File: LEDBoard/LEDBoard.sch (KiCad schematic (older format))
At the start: 0 parts

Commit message: added the LED board
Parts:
- added D?: LED-Green, symbol LED
- added R?: R, symbol R
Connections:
- new net: D?.2 (A), R?.2
- new net SOT2/Vout: D?.1 (K)
- new net VCC: R?.1
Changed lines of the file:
@@
 $Descr A4 11693 8268
 encoding utf-8
-Sheet 1 1
+Sheet 1 2
 Title "LED Board"
 Date "11-26-16"
@@
 Comment4 ""
 $EndDescr
+$Sheet
+S 2900 1800 700  500
+U 583A699B
+F0 "SOT2" 60
+F1 "SOT2.sch" 60
+F2 "Vin +" I L 2900 1900 60
+F3 "GND" I L 2900 2050 60
+F4 "Vin -" I L 2900 2200 60
+F5 "Vcc" I R 3600 1900 60
+F6 "Vout" O R 3600 2150 60
+$EndSheet
+$Comp
+L LED D?
+U 1 1 583A7260
+P 4250 2150
+F 0 "D?" H 4250 2250 50  0000 C CNN
+F 1 "LED-Green" H 4250 2050 50  0000 C CNN
+F 2 "" H 4250 2150 50  0000 C CNN
+F 3 "" H 4250 2150 50  0000 C CNN
+	1    4250 2150
+	1    0    0    -1
+$EndComp
+$Comp
+L R R?
+U 1 1 583A72AB
+P 5000 2150
+F 0 "R?" V 5080 2150 50  0000 C CNN
+F 1 "R" V 5000 2150 50  0000 C CNN
+F 2 "" V 4930 2150 50  0000 C CNN
+F 3 "" H 5000 2150 50  0000 C CNN
+	1    5000 2150
+	0    1    1    0
+$EndComp
+Wire Wire Line
+	4050 2150 3600 2150
+Wire Wire Line
+	4850 2150 4450 2150
+Wire Wire Line
+	5150 2150 5550 2150
+$Comp
+L VCC #PWR?
+U 1 1 583A734F
+P 5550 2150
+F 0 "#PWR?" H 5550 2000 50  0001 C CNN
+F 1 "VCC" H 5550 2300 50  0000 C CNN
+F 2 "" H 5550 2150 50  0000 C CNN
+F 3 "" H 5550 2150 50  0000 C CNN
+	1    5550 2150
+	0    1    1    0
+$EndComp
 $EndSCHEMATC

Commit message: just some updates to the LED Board
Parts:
- added BT-9V: Battery, symbol Battery
- added D?: LED-Green, symbol LED
- added R?: R, symbol R
- added U?: LM193, symbol LM193
- D?: value LED-Green -> LED-Red
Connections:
- net labels added: GND
- wire segments 3 -> 8
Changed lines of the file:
@@
 P 4250 2150
 F 0 "D?" H 4250 2250 50  0000 C CNN
-F 1 "LED-Green" H 4250 2050 50  0000 C CNN
+F 1 "LED-Red" H 4250 2050 50  0000 C CNN
 F 2 "" H 4250 2150 50  0000 C CNN
 F 3 "" H 4250 2150 50  0000 C CNN
@@
 	0    1    1    0
 $EndComp
+$Comp
+L Battery BT-9V
+U 1 1 583A7522
+P 7750 1200
+F 0 "BT-9V" H 7850 1250 50  0000 L CNN
+F 1 "Battery" H 7850 1150 50  0000 L CNN
+F 2 "" V 7750 1240 50  0000 C CNN
+F 3 "" V 7750 1240 50  0000 C CNN
+	1    7750 1200
+	0    1    1    0
+$EndComp
+$Comp
+L GND #PWR?
+U 1 1 583A756B
+P 7450 1200
+F 0 "#PWR?" H 7450 950 50  0001 C CNN
+F 1 "GND" H 7450 1050 50  0000 C CNN
+F 2 "" H 7450 1200 50  0000 C CNN
+F 3 "" H 7450 1200 50  0000 C CNN
+	1    7450 1200
+	0    1    1    0
+$EndComp
+Wire Wire Line
+	7600 1200 7450 1200
+$Comp
+L R R?
+U 1 1 583A7609
+P 5000 1850
+F 0 "R?" V 5080 1850 50  0000 C CNN
+F 1 "R" V 5000 1850 50  0000 C CNN
+F 2 "" V 4930 1850 50  0000 C CNN
+F 3 "" H 5000 1850 50  0000 C CNN
+	1    5000 1850
+	0    1    1    0
+$EndComp
+$Comp
+L LED D?
+U 1 1 583A765A
+P 4500 1850
+F 0 "D?" H 4500 1950 50  0000 C CNN
+F 1 "LED-Green" H 4500 1750 50  0000 C CNN
+F 2 "" H 4500 1850 50  0000 C CNN
+F 3 "" H 4500 1850 50  0000 C CNN
+	1    4500 1850
+	1    0    0    -1
+$EndComp
+$Comp
+L GND #PWR?
+U 1 1 583A769A
+P 4200 1850
+F 0 "#PWR?" H 4200 1600 50  0001 C CNN
+F 1 "GND" H 4200 1700 50  0000 C CNN
+F 2 "" H 4200 1850 50  0000 C CNN
+F 3 "" H 4200 1850 50  0000 C CNN
+	1    4200 1850
+	0    1    1    0
+$EndComp
+Wire Wire Line
+	5350 2150 5350 1850
+Wire Wire Line
+	5350 1850 5150 1850
+Connection ~ 5350 2150
+Wire Wire Line
+	4850 1850 4700 1850
+Wire Wire Line
+	4300 1850 4200 1850
+$Comp
+L LM193 U?
+U 1 1 583A7B90
+P 10000 1250
+F 0 "U?" H 10150 1400 50  0000 C CNN
+F 1 "LM193" H 10250 1100 50  0000 C CNN
+F 2 "" H 10000 1250 50  0000 C CNN
+F 3 "" H 10000 1250 50  0000 C CNN
+	1    10000 1250
+	1    0    0    -1
+$EndComp
 $EndSCHEMATC

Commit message: more work on the LED board
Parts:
- removed BT-9V: Battery, symbol Battery
- removed D?: LED-Red, symbol LED
- removed D?: LED-Green, symbol LED
- removed R? (x2): R, symbol R
- removed U?: LM193, symbol LM193
- added P?: connector to 9V battery, symbol CONN_01X02
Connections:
- net labels removed: GND, VCC
- wire segments 8 -> 0

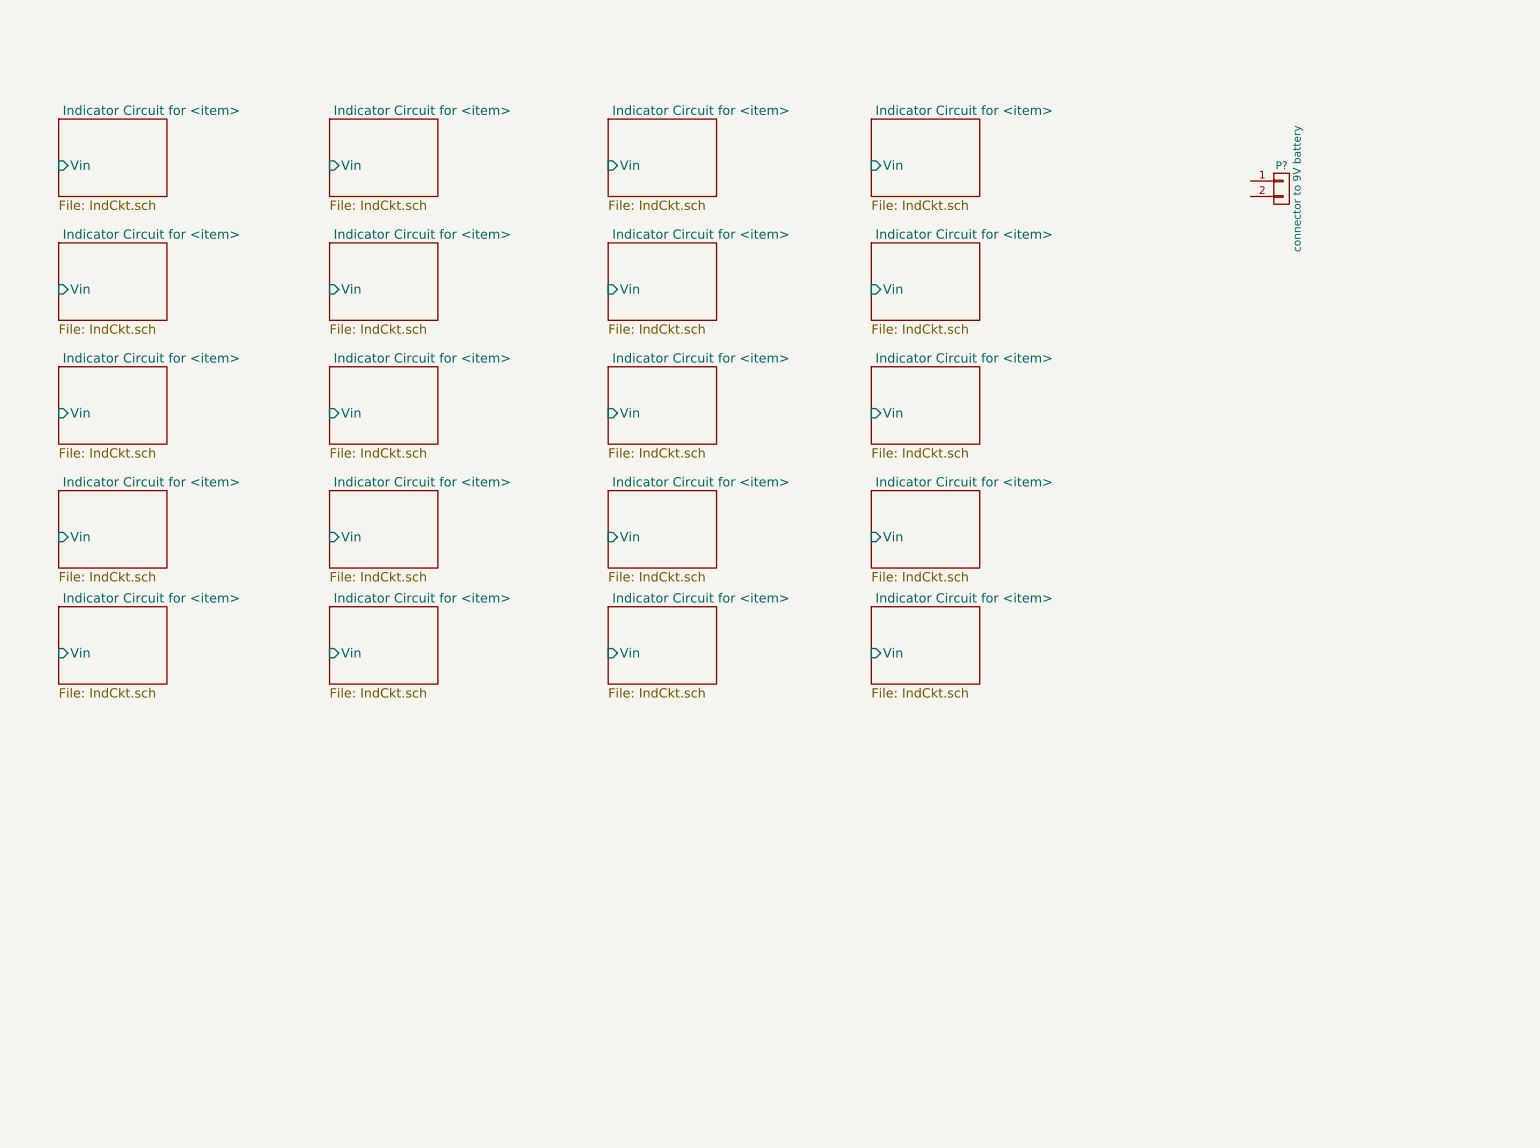
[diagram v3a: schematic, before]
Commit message: Added the power switching device and wiring between the pod batteries and backup batteries
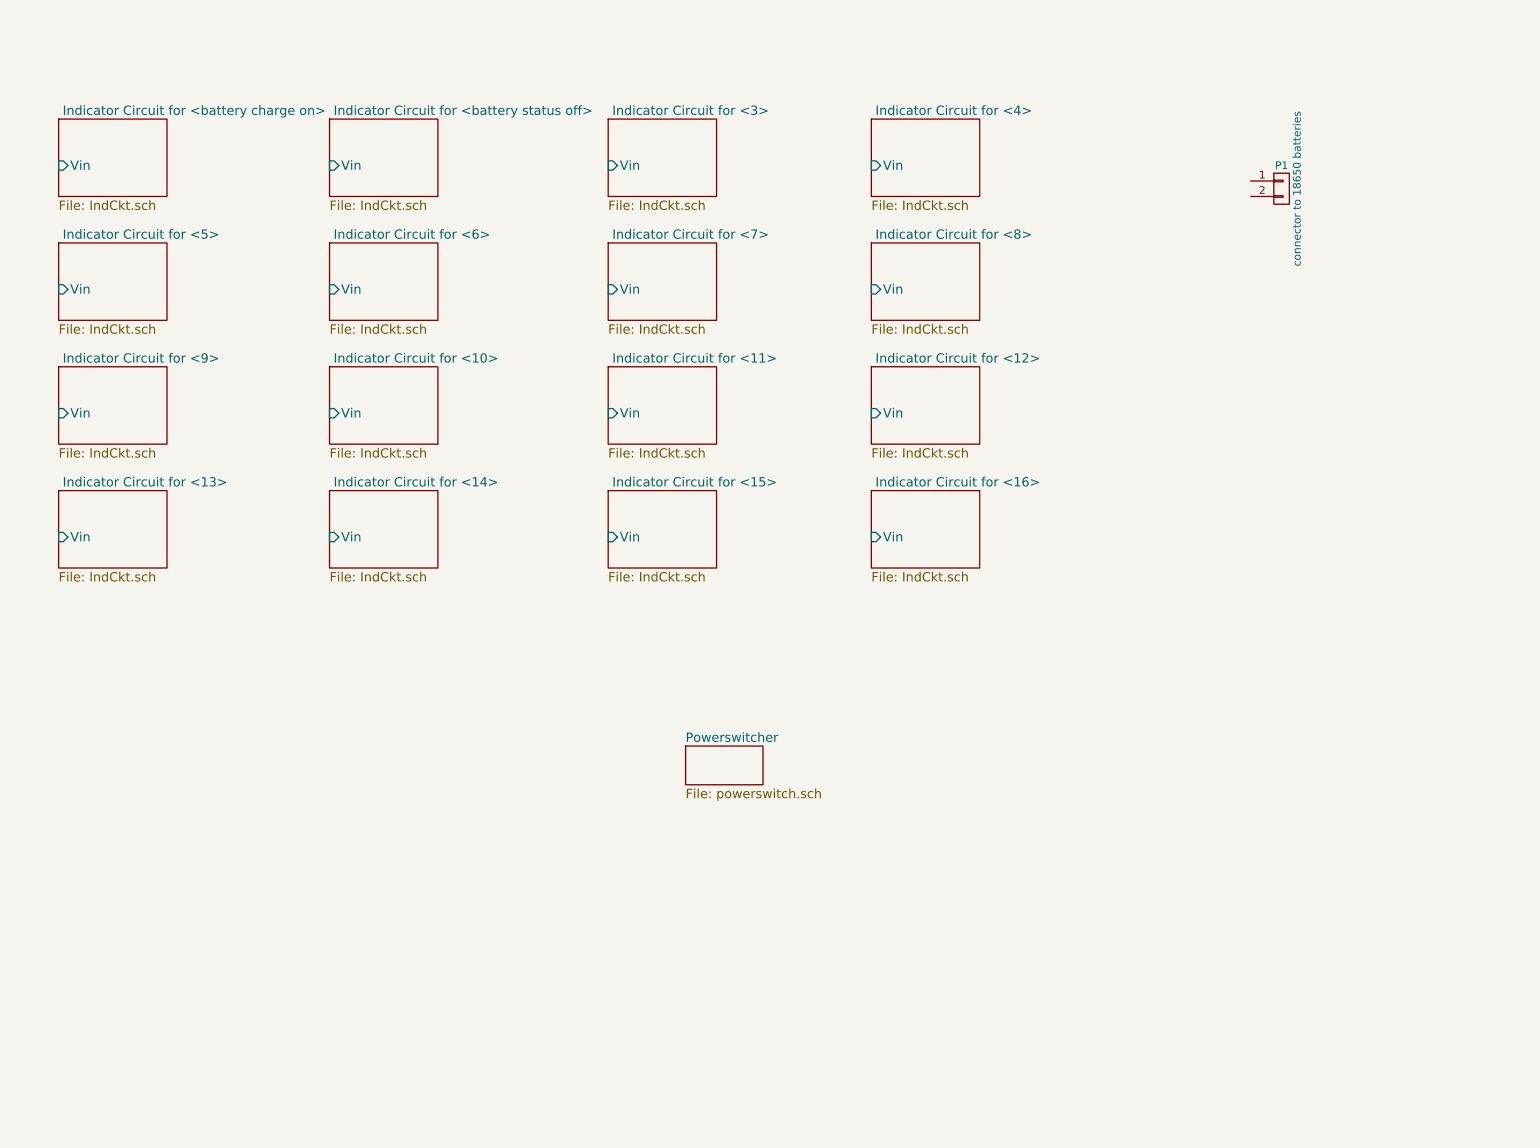
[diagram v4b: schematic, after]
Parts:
- P1: renamed from P?; value connector to 9V battery -> connector to 18650 batteries
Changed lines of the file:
@@
 LIBS:contrib
 LIBS:valves
+LIBS:SOT2-cache
 LIBS:LEDBoard-cache
 EELAYER 25 0
@@
 $Descr A4 11693 8268
 encoding utf-8
-Sheet 1 21
+Sheet 1 18
 Title "LED Board"
 Date "11-26-16"
@@
 S 1100 1300 700  500
 U 583A699B
-F0 " Indicator Circuit for <item>" 60
+F0 " Indicator Circuit for <battery charge on>" 60
 F1 "IndCkt.sch" 60
 F2 "Vin" I L 1100 1600 60
@@
 S 1100 2100 700  500
 U 583ACA1C
-F0 " Indicator Circuit for <item>" 60
+F0 " Indicator Circuit for <5>" 60
 F1 "IndCkt.sch" 60
 F2 "Vin" I L 1100 2400 60
@@
 S 1100 2900 700  500
 U 583ACAFB
-F0 " Indicator Circuit for <item>" 60
+F0 " Indicator Circuit for <9>" 60
 F1 "IndCkt.sch" 60
 F2 "Vin" I L 1100 3200 60
@@
 S 1100 3700 700  500
 U 583ACAFE
-F0 " Indicator Circuit for <item>" 60
+F0 " Indicator Circuit for <13>" 60
 F1 "IndCkt.sch" 60
 F2 "Vin" I L 1100 4000 60
 $EndSheet
 $Sheet
-S 1100 4450 700  500
-U 583ACB74
-F0 " Indicator Circuit for <item>" 60
-F1 "IndCkt.sch" 60
-F2 "Vin" I L 1100 4750 60
-$EndSheet
-$Sheet
 S 2850 1300 700  500
 U 583ACE7E
-F0 " Indicator Circuit for <item>" 60
+F0 " Indicator Circuit for <battery status off>" 60
 F1 "IndCkt.sch" 60
 F2 "Vin" I L 2850 1600 60
@@
 S 2850 2100 700  500
 U 583ACE81
-F0 " Indicator Circuit for <item>" 60
+F0 " Indicator Circuit for <6>" 60
 F1 "IndCkt.sch" 60
 F2 "Vin" I L 2850 2400 60
@@
 S 2850 2900 700  500
 U 583ACE84
-F0 " Indicator Circuit for <item>" 60
+F0 " Indicator Circuit for <10>" 60
 F1 "IndCkt.sch" 60
 F2 "Vin" I L 2850 3200 60
@@
 S 2850 3700 700  500
 U 583ACE87
-F0 " Indicator Circuit for <item>" 60
+F0 " Indicator Circuit for <14>" 60
 F1 "IndCkt.sch" 60
 F2 "Vin" I L 2850 4000 60
 $EndSheet
 $Sheet
-S 2850 4450 700  500
-U 583ACE8A
-F0 " Indicator Circuit for <item>" 60
-F1 "IndCkt.sch" 60
-F2 "Vin" I L 2850 4750 60
-$EndSheet
-$Sheet
 S 4650 1300 700  500
 U 583AD5B9
-F0 " Indicator Circuit for <item>" 60
+F0 " Indicator Circuit for <3>" 60
 F1 "IndCkt.sch" 60
 F2 "Vin" I L 4650 1600 60
@@
 S 4650 2100 700  500
 U 583AD5BC
-F0 " Indicator Circuit for <item>" 60
+F0 " Indicator Circuit for <7>" 60
 F1 "IndCkt.sch" 60
 F2 "Vin" I L 4650 2400 60
@@
 S 4650 2900 700  500
 U 583AD5BF
-F0 " Indicator Circuit for <item>" 60
+F0 " Indicator Circuit for <11>" 60
 F1 "IndCkt.sch" 60
 F2 "Vin" I L 4650 3200 60
@@
 S 4650 3700 700  500
 U 583AD5C2
-F0 " Indicator Circuit for <item>" 60
+F0 " Indicator Circuit for <15>" 60
 F1 "IndCkt.sch" 60
 F2 "Vin" I L 4650 4000 60
 $EndSheet
 $Sheet
-S 4650 4450 700  500
-U 583AD5C5
-F0 " Indicator Circuit for <item>" 60
-F1 "IndCkt.sch" 60
-F2 "Vin" I L 4650 4750 60
-$EndSheet
-$Sheet
 S 6350 1300 700  500
 U 583AD5C8
-F0 " Indicator Circuit for <item>" 60
+F0 " Indicator Circuit for <4>" 60
 F1 "IndCkt.sch" 60
 F2 "Vin" I L 6350 1600 60
@@
 S 6350 2100 700  500
 U 583AD5CB
-F0 " Indicator Circuit for <item>" 60
+F0 " Indicator Circuit for <8>" 60
 F1 "IndCkt.sch" 60
 F2 "Vin" I L 6350 2400 60
@@
 S 6350 2900 700  500
 U 583AD5CE
-F0 " Indicator Circuit for <item>" 60
+F0 " Indicator Circuit for <12>" 60
 F1 "IndCkt.sch" 60
 F2 "Vin" I L 6350 3200 60
@@
 S 6350 3700 700  500
 U 583AD5D1
-F0 " Indicator Circuit for <item>" 60
+F0 " Indicator Circuit for <16>" 60
 F1 "IndCkt.sch" 60
 F2 "Vin" I L 6350 4000 60
 $EndSheet
-$Sheet
-S 6350 4450 700  500
-U 583AD5D4
-F0 " Indicator Circuit for <item>" 60
-F1 "IndCkt.sch" 60
-F2 "Vin" I L 6350 4750 60
-$EndSheet
 $Comp
-L CONN_01X02 P?
+L CONN_01X02 P1
 U 1 1 583ADF07
 P 9000 1750
-F 0 "P?" H 9000 1900 50  0000 C CNN
-F 1 "connector to 9V battery" V 9100 1750 50  0000 C CNN
+F 0 "P1" H 9000 1900 50  0000 C CNN
+F 1 "connector to 18650 batteries" V 9100 1750 50  0000 C CNN
 F 2 "" H 9000 1750 50  0000 C CNN
 F 3 "" H 9000 1750 50  0000 C CNN
@@
 	1    0    0    -1
 $EndComp
+$Sheet
+S 5150 5350 500  250
+U 584C88BC
+F0 "Powerswitcher" 60
+F1 "powerswitch.sch" 60
+$EndSheet
 $EndSCHEMATC

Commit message: made major changed to the led board mostly dealing with schematic
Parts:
- added P101, P102, P103, P104, P105, P106: CONN_01X02, hyperCustom:CONN_PHOENIX_1844210_2PIN, symbol CONN_01X02
- added P108, P?: CONN_01X04, hyperCustom:CONN_PHOENIX_1844236_4PIN_1, symbol CONN_01X04
- added P109: CONN_01X06, hyperCustom:CONN_PHOENIX_1844252_6PIN, symbol CONN_01X06
- P107: renamed from P1; footprint (none) -> hyperCustom:CONN_PHOENIX_1844210_2PIN
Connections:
- net Auxiliary_Bat: now reaches P107.1 (P1)
- net GND: now reaches P107.2 (P2)
- net GND: now also P101.2 (P2), P102.2 (P2), P103.2 (P2), P104.2 (P2), P105.2 (P2), P106.2 (P2), P108.3 (P3), P108.4 (P4), P109.4 (P4), P109.5 (P5), P109.6 (P6), P?.4 (P4)
- new net Ind1: P101.1 (P1)
- new net Ind2: P102.1 (P1)
- new net Ind3: P103.1 (P1)
- new net Ind4: P104.1 (P1)
- new net Ind5: P105.1 (P1)
- new net Ind6: P106.1 (P1)
- new net Merkl2: P108.2 (P2)
- new net MerklState: P108.1 (P1)
- new net PowerBoard: P109.3 (P3)
- new net State: P109.1 (P1)
- new net Vbat: P109.2 (P2)

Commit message: akdhf
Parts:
- gave numbers to parts that had none: 1
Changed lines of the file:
@@
 Auxiliary_Bat
 $Comp
-L GND #PWR107
+L GND #PWR108
 U 1 1 58518298
 P 8800 1800
-F 0 "#PWR107" H 8800 1550 50  0001 C CNN
+F 0 "#PWR108" H 8800 1550 50  0001 C CNN
 F 1 "GND" H 8800 1650 50  0000 C CNN
 F 2 "" H 8800 1800 50  0000 C CNN
@@
 $EndComp
 $Comp
-L GND #PWR110
+L GND #PWR111
 U 1 1 58519412
 P 9250 3100
-F 0 "#PWR110" H 9250 2850 50  0001 C CNN
+F 0 "#PWR111" H 9250 2850 50  0001 C CNN
 F 1 "GND" H 9250 2950 50  0000 C CNN
 F 2 "" H 9250 3100 50  0000 C CNN
@@
 $EndComp
 $Comp
-L GND #PWR111
+L GND #PWR112
 U 1 1 5851948A
 P 9250 3200
-F 0 "#PWR111" H 9250 2950 50  0001 C CNN
+F 0 "#PWR112" H 9250 2950 50  0001 C CNN
 F 1 "GND" H 9250 3050 50  0000 C CNN
 F 2 "" H 9250 3200 50  0000 C CNN
@@
 $EndComp
 $Comp
-L GND #PWR112
+L GND #PWR113
 U 1 1 585194FB
 P 9250 3300
-F 0 "#PWR112" H 9250 3050 50  0001 C CNN
+F 0 "#PWR113" H 9250 3050 50  0001 C CNN
 F 1 "GND" H 9250 3150 50  0000 C CNN
 F 2 "" H 9250 3300 50  0000 C CNN
@@
 	9200 4950 8750 4950
 $Comp
-L GND #PWR108
+L GND #PWR109
 U 1 1 5851C10C
 P 9200 5050
-F 0 "#PWR108" H 9200 4800 50  0001 C CNN
+F 0 "#PWR109" H 9200 4800 50  0001 C CNN
 F 1 "GND" H 9200 4900 50  0000 C CNN
 F 2 "" H 9200 5050 50  0000 C CNN
@@
 $EndComp
 $Comp
-L GND #PWR109
+L GND #PWR110
 U 1 1 5851C2B1
 P 9200 5150
-F 0 "#PWR109" H 9200 4900 50  0001 C CNN
+F 0 "#PWR110" H 9200 4900 50  0001 C CNN
 F 1 "GND" H 9200 5000 50  0000 C CNN
 F 2 "" H 9200 5150 50  0000 C CNN
@@
 Ind6
 $Comp
-L CONN_01X04 P?
+L CONN_01X04 P110
 U 1 1 58520193
 P 7650 5250
-F 0 "P?" H 7650 5500 50  0000 C CNN
+F 0 "P110" H 7650 5500 50  0000 C CNN
 F 1 "CONN_01X04" V 7750 5250 50  0000 C CNN
 F 2 "hyperCustom:CONN_PHOENIX_1844236_4PIN_1" H 7650 5250 50  0001 C CNN
@@
 $EndComp
 $Comp
-L GND #PWR?
+L GND #PWR107
 U 1 1 585203A3
 P 7450 5400
-F 0 "#PWR?" H 7450 5150 50  0001 C CNN
+F 0 "#PWR107" H 7450 5150 50  0001 C CNN
 F 1 "GND" H 7450 5250 50  0000 C CNN
 F 2 "" H 7450 5400 50  0000 C CNN
